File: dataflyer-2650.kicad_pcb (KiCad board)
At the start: 2 copper layers, 73.5 x 35 mm, 2 parts, among them J1 26-pin IDC (Dataflyer side), J2 50-pin IDC (SCSI chain out)

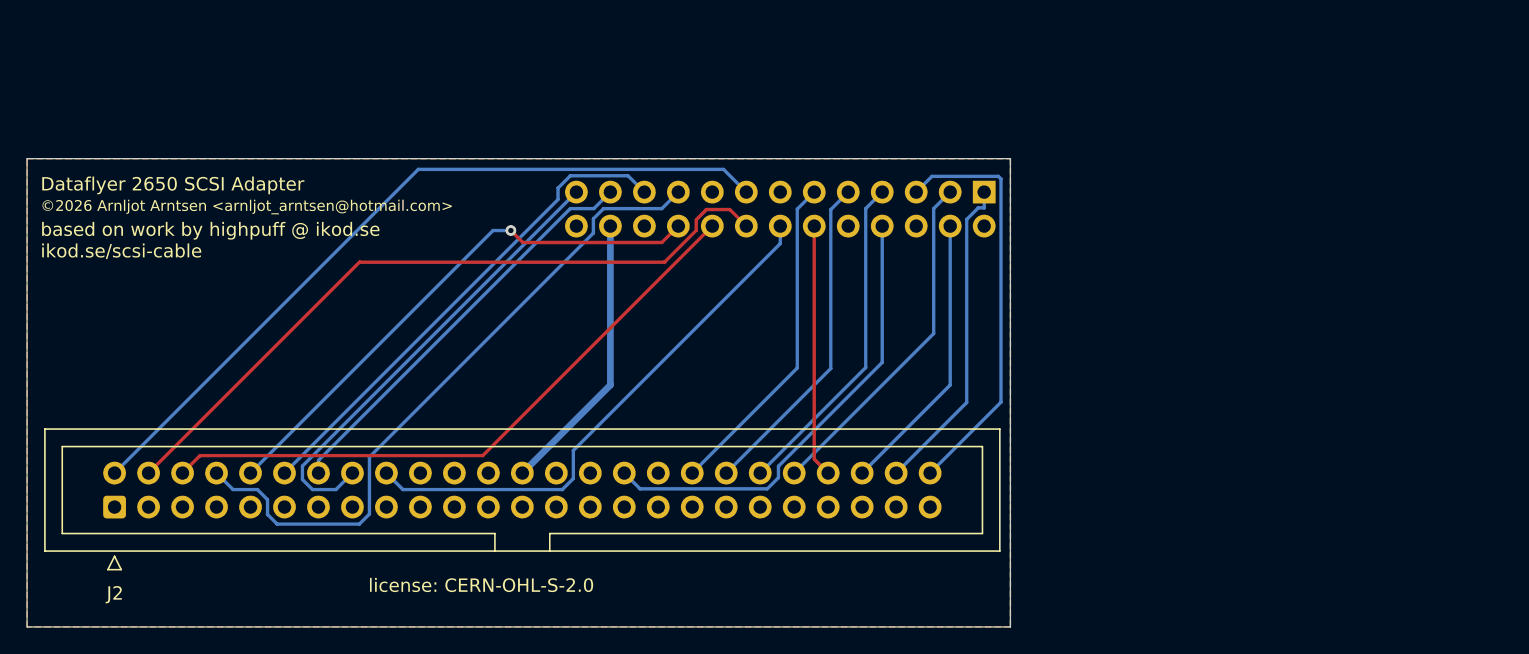
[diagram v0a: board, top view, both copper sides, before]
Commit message: Release 1.1: GND reserved IDC50 pins; J1 moved inboard
Schematic: connect SCSI-1 reserved IDC50 pins 20, 22, 24, 28, 30, 34
to GND for cleaner signaling and to match common SCSI-1 controller
practice (these were left floating in 1.0).

PCB: J1 shifted ~3.5 mm inboard for easier routing. Board outline
(73.5 x 35 mm) and connector mating are unchanged — does not affect
fit with DataFlyer 1200 SCSI+ or Phase5 Blizzard IV SCSI kit.

Docs: README revision history, PINOUT.md IDC50 ground net section.
KiCad schematic rev bumped 1.0 -> 1.1 (PCB internal rev left at 1.8).
Freerouting artifacts (.dsn/.ses/.rules) re-exported.

(c) 2026 Arnljot Arntsen
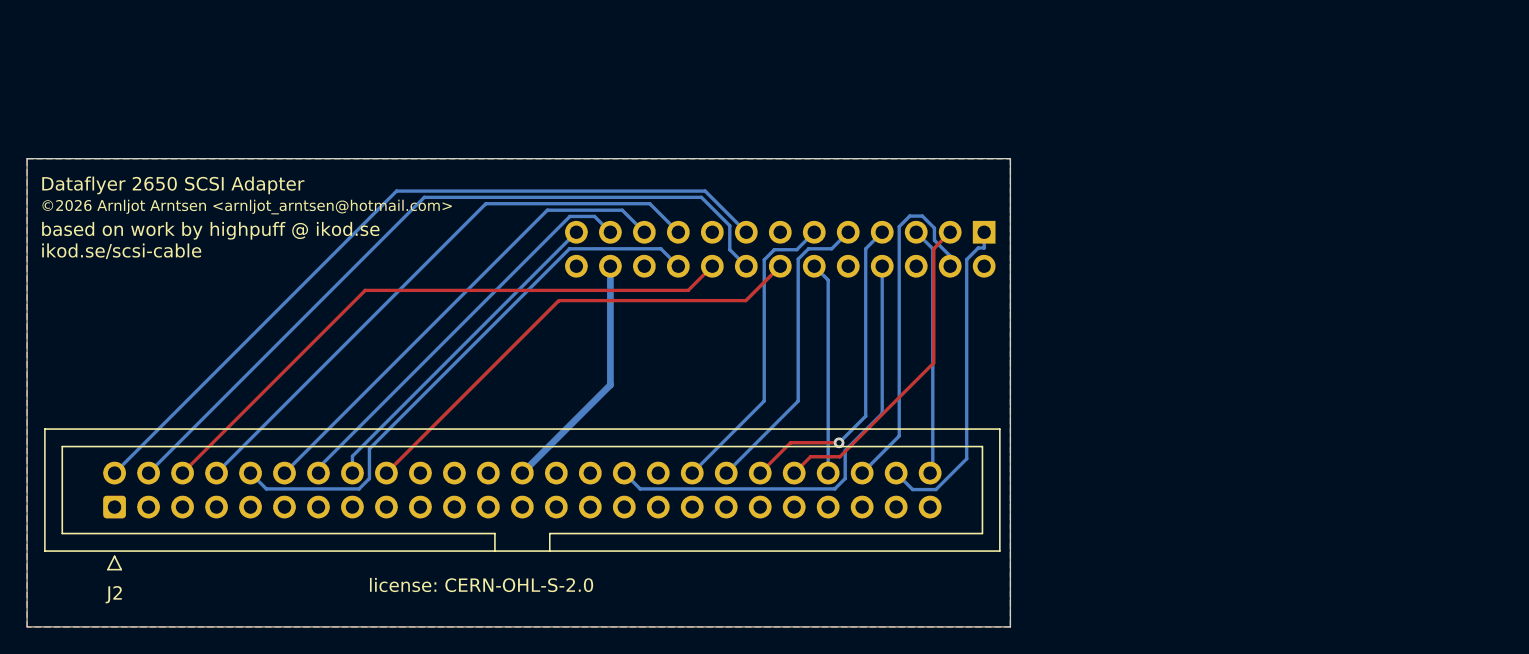
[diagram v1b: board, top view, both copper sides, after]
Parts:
- moved J1 3.00 mm to (135.5, 105.5)
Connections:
- J2 pad 20: unconnected-(J2-Pin_20-Pad20) -> GND
- J2 pad 22: unconnected-(J2-Pin_22-Pad22) -> GND
- J2 pad 24: unconnected-(J2-Pin_24-Pad24) -> GND
- J2 pad 28: unconnected-(J2-Pin_28-Pad28) -> GND
- J2 pad 30: unconnected-(J2-Pin_30-Pad30) -> GND
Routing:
- net IO: track 31.1 -> 18.6 mm
- net DB7: track 34.5 -> 24.9 mm
- net DB3: track 50.2 -> 43.7 mm
- net CD: track 21.2 -> 26.2 mm
- net DBP: track 40.1 -> 35.8 mm
- net TERMPWR: track 21.2 -> 18.2 mm
- net SEL: track 18.9 -> 15.9 mm
- net DB1: track 53.8 -> 56.4 mm
- net BSY: track 24.8 -> 22.8 mm
- net ACK: track 24.8 -> 22.8 mm
- net MSG: track 25.8 -> 24.1 mm
- net DB5: track 37.1 -> 35.7 mm
- net DB4: track 40.4 -> 41.7 mm, vias 1 -> 0
- net DB2: track 47.2 -> 46.0 mm
- net RST: track 24.8 -> 23.9 mm, vias 0 -> 1
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
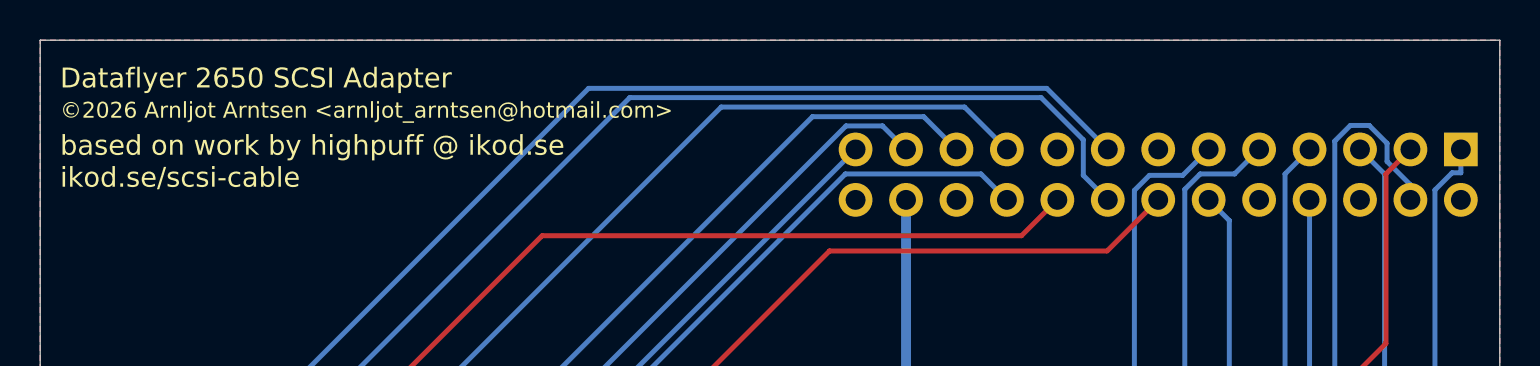
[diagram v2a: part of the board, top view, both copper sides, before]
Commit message: 1.1.1: project text variables + silkscreen overhaul + J1 pin 1 marker
Project text variables (.kicad_pro):
- BOARD_NAME = "DataFlyer 2650 — 26-pin to 50-pin SCSI Adapter"
- BOARD_REV  = "1.1.1"
- sch_revision now references ${BOARD_REV}
- Plot output directory set to gerbers/

Schematic (.kicad_sch):
- title and rev fields now reference ${BOARD_NAME} / ${BOARD_REV}
  so the project text variables are the single source of truth

PCB (.kicad_pcb):
- Board-level BOARD_NAME and BOARD_REV properties added
- Front silkscreen overhauled:
  * Board name now uses ${BOARD_NAME} (fixes lingering lowercase
    "Dataflyer 2650 SCSI Adapter" instance)
  * Added "Rev ${BOARD_REV}" line
  * Added "github.com/arnljot/dataflyer2650" repo URL
  * Attribution split into two readable lines:
    "based on work by highpuff @ ikod.se" / "ikod.se/scsi-cable"
- J1 pin 1 marker added on B.Cu (bottom copper, mirrored, bold 1.5mm)
  for permanent indication on the underside that mates with the
  controller card's male header
- Plot output directory set to gerbers/

Patch release per the new release policy: lives on main, no GitHub
release tag.

(c) 2026 Arnljot Arntsen
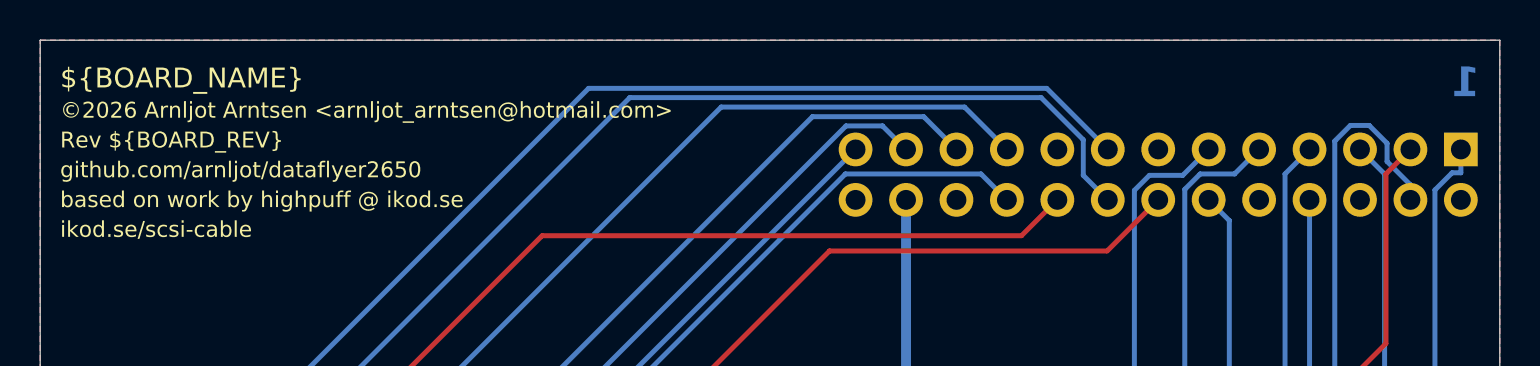
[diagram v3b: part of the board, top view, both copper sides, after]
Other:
- board text added: "${BOARD_NAME}"
- board text added: "1"
- board text added: "Rev ${BOARD_REV}"
- board text added: "based on work by highpuff @ ikod.se"
- board text added: "github.com/arnljot/dataflyer2650"
- board text added: "ikod.se/scsi-cable"
- board text removed: "Dataflyer 2650 SCSI Adapter"
- board text removed: "based on work by highpuff @ ikod.se ikod.se/scsi-cable"
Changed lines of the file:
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@@
 			(outputformat 1)
 			(mirror no)
-			(drillshape 1)
+			(drillshape 0)
 			(scaleselection 1)
-			(outputdirectory "")
+			(outputdirectory "gerbers/")
 		)
 	)
+	(property "BOARD_NAME" "DataFlyer 2650 — 26-pin to 50-pin SCSI Adapter")
+	(property "BOARD_REV" "1.1.1")
 	(footprint "Connector_IDC:IDC-Header_2x25_P2.54mm_Vertical"
 		(layer "F.Cu")
@@
 		(layer "Edge.Cuts")
 	)
+	(gr_text "1"
+		(at 136.5 103 0)
+		(layer "B.Cu")
+		(effects
+			(font
+				(size 1.5 1.5)
+				(thickness 0.3)
+				(bold yes)
+			)
+			(justify left bottom mirror)
+		)
+	)
 	(gr_text "©2026 Arnljot Arntsen <arnljot_arntsen@hotmail.com>"
 		(at 65 104 0)
@@
 		)
 	)
-	(gr_text "Dataflyer 2650 SCSI Adapter"
+	(gr_text "Rev ${BOARD_REV}"
+		(at 65 105.5 0)
+		(layer "F.SilkS")
+		(effects
+			(font
+				(size 0.8 0.8)
+				(thickness 0.1)
+			)
+			(justify left bottom)
+		)
+	)
+	(gr_text "github.com/arnljot/dataflyer2650"
+		(at 65 107 0)
+		(layer "F.SilkS")
+		(effects
+			(font
+				(size 0.8 0.8)
+				(thickness 0.1)
+			)
+			(justify left bottom)
+		)
+	)
+	(gr_text "based on work by highpuff @ ikod.se"
+		(at 65 108.5 0)
+		(layer "F.SilkS")
+		(effects
+			(font
+				(size 0.8 0.8)
+				(thickness 0.1)
+			)
+			(justify left bottom)
+		)
+	)
+	(gr_text "ikod.se/scsi-cable"
+		(at 65 110 0)
+		(layer "F.SilkS")
+		(effects
+			(font
+				(size 0.8 0.8)
+				(thickness 0.1)
+			)
+			(justify left bottom)
+		)
+	)
+	(gr_text "${BOARD_NAME}"
 		(at 65 102.5 0)
 		(layer "F.SilkS")
 		(effects
-			(font
-				(size 1 1)
-				(thickness 0.15)
-			)
-			(justify left bottom)
-		)
-	)
-	(gr_text "based on work by highpuff @ ikod.se\nikod.se/scsi-cable"
-		(at 65 107.5 0)
-		(layer "F.SilkS")
-		(effects

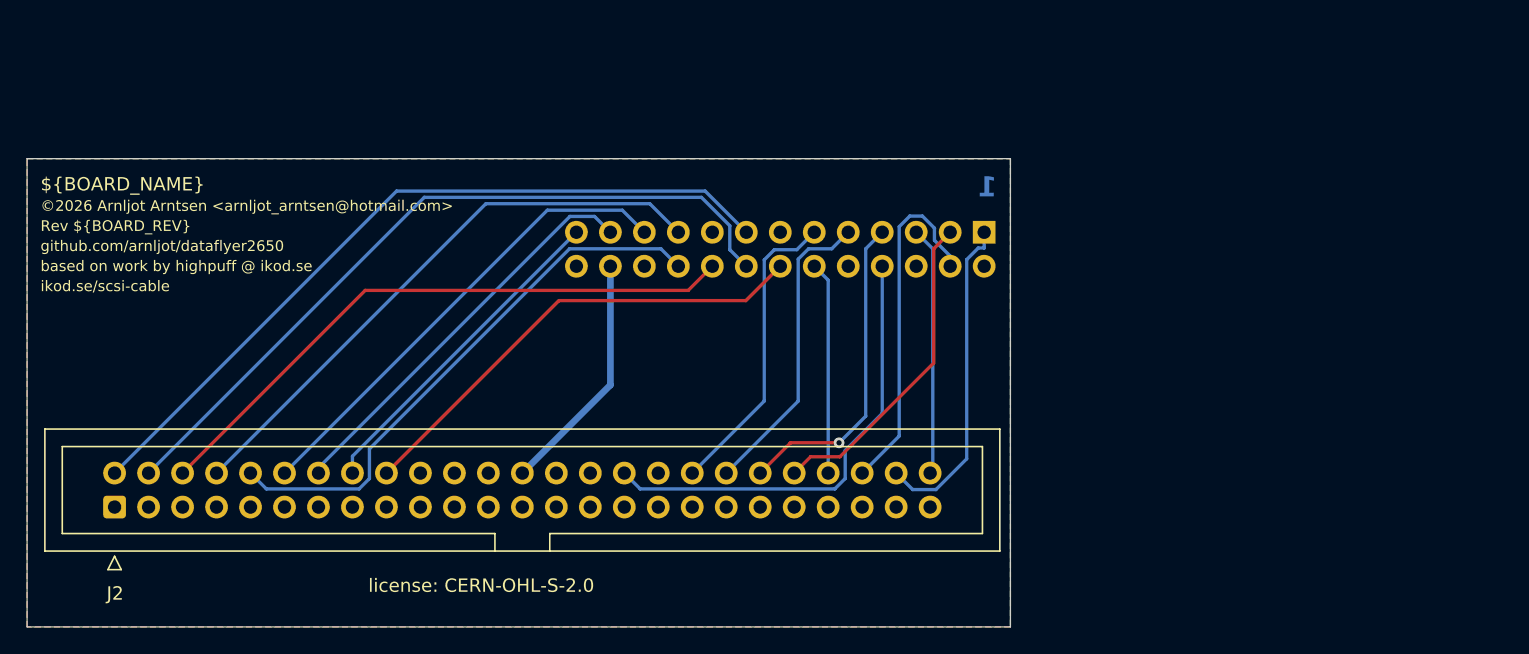
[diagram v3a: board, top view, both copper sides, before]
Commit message: 1.2: reverse-L board outline that wraps around the Blizzard SCSI kit
The rectangular 1.1/1.1.1 outline would not clear a wedge Amiga 1200
fitted with a Phase5 Blizzard accelerator. The board has been reshaped
to a reverse-L outline (79.05 x 26.01 mm) that wraps around the Blizzard
SCSI kit: a full-width top band carries the 50-pin J2, the board extends
down only on the right to form a tab carrying the 26-pin J1, and the
lower-left corner is removed.

Fit reasoning:
- J2 (50-pin) is pushed further toward the rear of the A1200 to keep the
  SCSI cable clear of the keyboard where the case tapers to the front.
- For DataFlyer 1200 SCSI+ mounting, the area to the left of the 26-pin
  connector (toward the PCMCIA slot) is minimized as far as possible to
  avoid fouling the A1200 RF shielding.
- Known limitation: the SCSI cable still exits to the left; a future
  revision may rotate J2 180 degrees so the cable clears the RF
  shielding.

Schematic and pinout are unchanged from 1.1.1 — outline/layout change
only, electrically identical.

Hardware status:
- Tested working in an Amiga 1200 with the Phase5 Blizzard IV SCSI kit.
- Not yet tested in the Expansion Systems DataFlyer 1200 SCSI+.

Files:
- KiCad sources updated (.kicad_pcb, .kicad_pro, .dsn, .ses);
  BOARD_REV = 1.2.
- Gerbers + drill re-exported from KiCad 10.0.3.
- Bundled zip (dataflyer-2650-v1.2.zip) submitted to PCBWay.
- README revision history updated; Files section rev numbers synced.

(c) 2026 Arnljot Arntsen
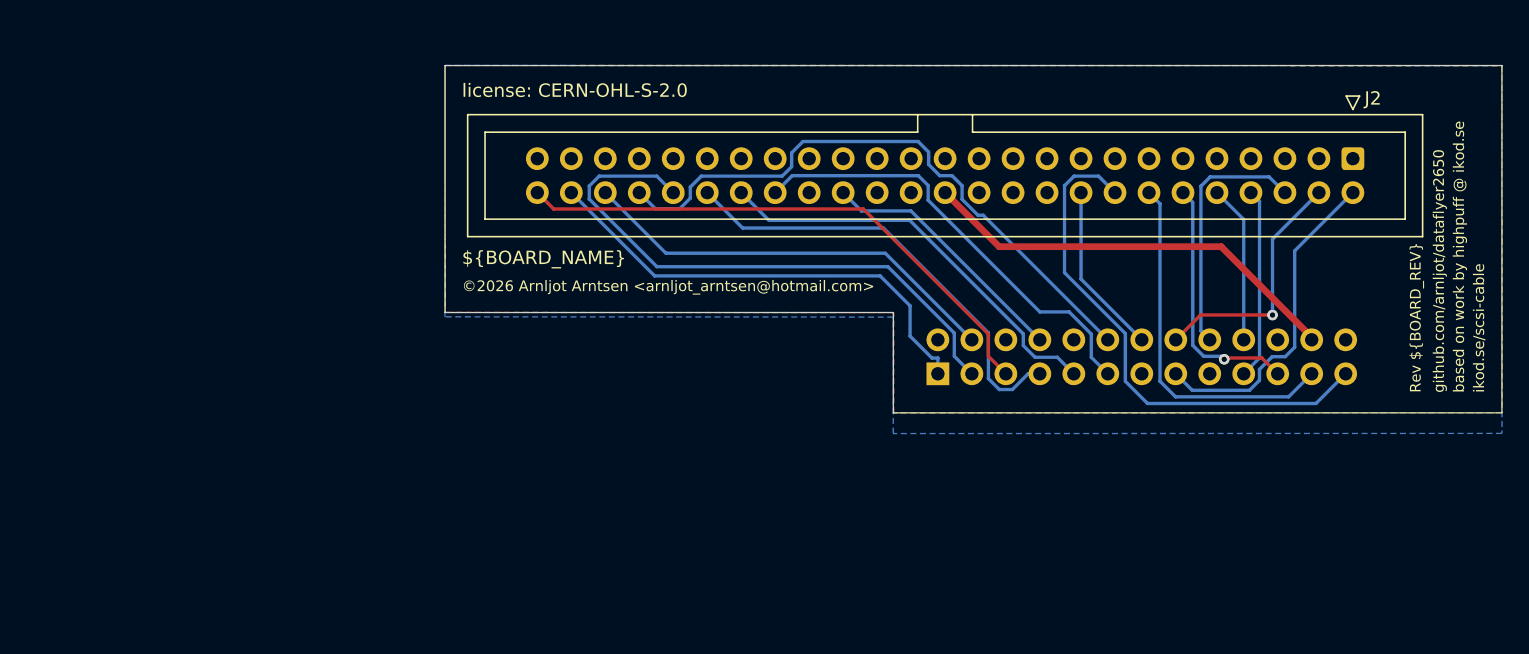
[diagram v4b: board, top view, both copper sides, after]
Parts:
- moved J2 96.2 mm to (163.1, 100.0), turned to -90 degrees
- moved J1 11.1 mm to (132.1, 116.1), turned to -90 degrees
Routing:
- net DB1: track 56.4 -> 18.6 mm, vias 0 -> 1
- net DB0: track 57.2 -> 24.6 mm
- net SEL: track 15.9 -> 46.0 mm
- net DB4: track 41.7 -> 11.8 mm
- net DB3: track 43.7 -> 14.3 mm
- net DB2: track 46.0 -> 18.8 mm
- net IO: track 18.6 -> 41.6 mm
- net DBP: track 35.8 -> 12.9 mm
- net MSG: track 24.1 -> 43.1 mm
- net DB5: track 35.7 -> 19.0 mm, vias 0 -> 1
- net ATN: track 34.3 -> 19.3 mm
- net DB7: track 24.9 -> 39.2 mm
- net TERMPWR: track 18.2 -> 32.1 mm
- net REQ: track 24.5 -> 35.0 mm
- net BSY: track 22.8 -> 33.2 mm
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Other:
- board size 73.5 x 35 mm -> 79 x 26 mm
- board text removed: "1"
